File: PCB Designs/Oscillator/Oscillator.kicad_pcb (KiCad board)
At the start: 2 copper layers, 7 parts, among them Q3 2N2222A, Q4 2N2222A

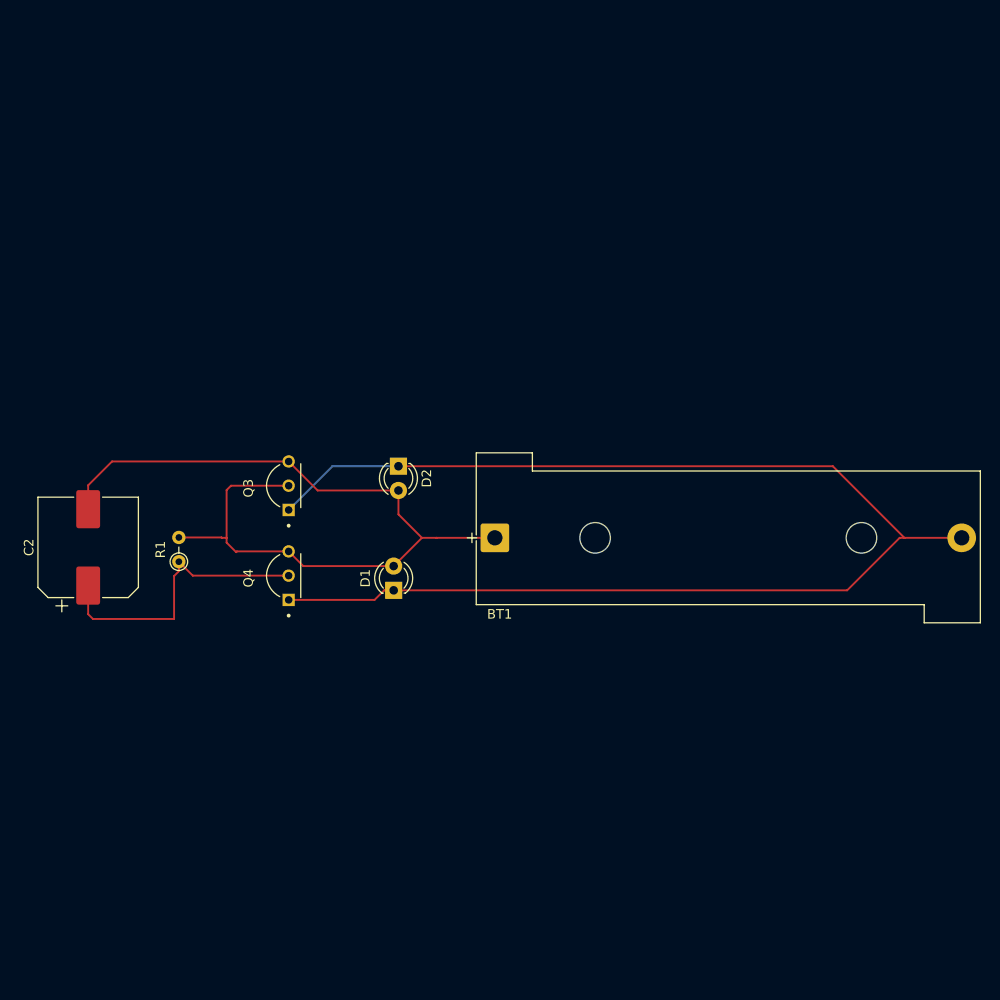
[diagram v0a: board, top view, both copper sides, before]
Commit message: Developed upon esp 32 schem
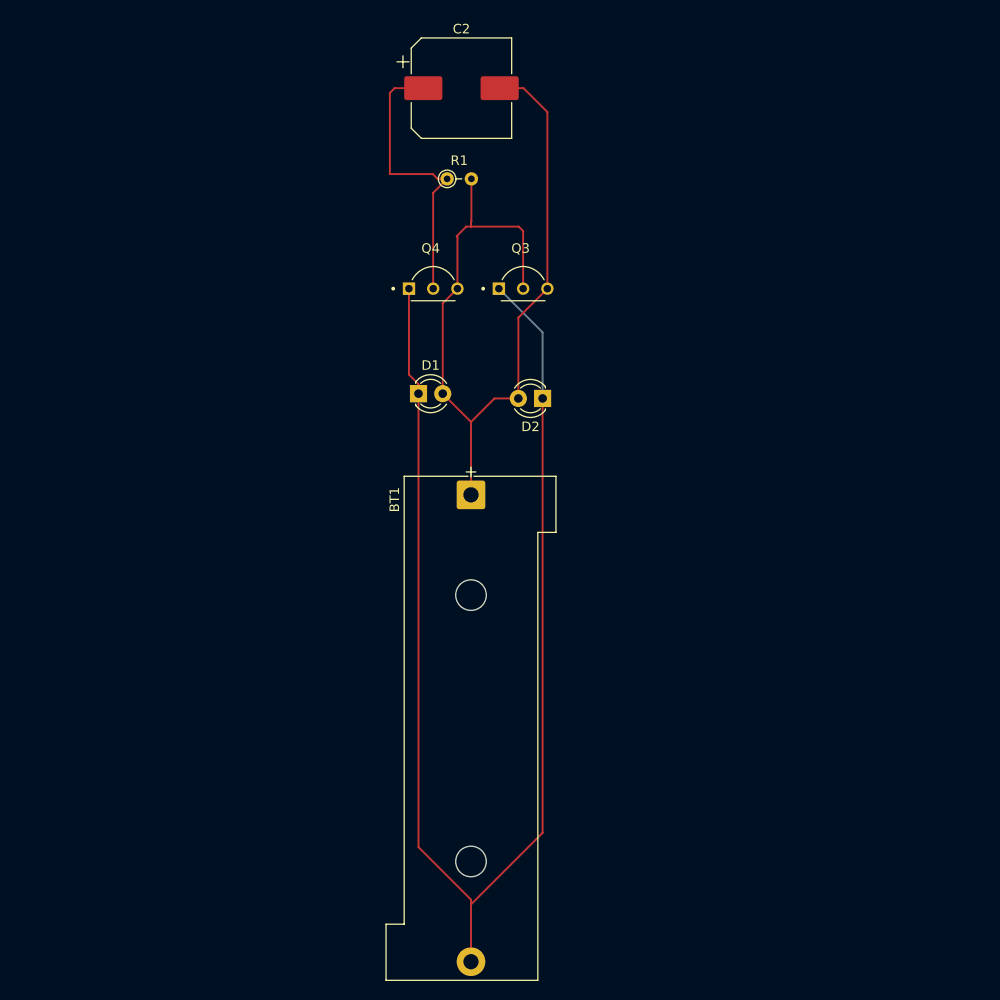
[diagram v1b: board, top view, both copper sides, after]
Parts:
- moved C2 62.0 mm to (94.1, 61.9), turned to 0 degrees
- moved R1 49.0 mm to (92.6, 71.4), turned to 0 degrees
- moved Q4 36.8 mm to (91.1, 80.6), turned to 0 degrees
- moved Q3 35.4 mm to (100.6, 80.6), turned to 0 degrees
- moved D1 20.8 mm to (89.6, 93.9), turned to 0 degrees
- moved D2 16.7 mm to (102.6, 94.4), turned to 180 degrees
- moved BT1 5.15 mm to (95.1, 104.5), turned to -90 degrees
